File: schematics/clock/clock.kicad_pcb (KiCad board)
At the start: 2 copper layers, 102 x 96 mm, 25 parts, among them J1 Bus, J2 Bus, SW1 RUN, SW2 PULSE, U1 NE556, U2 74LS27, U3 74LS27

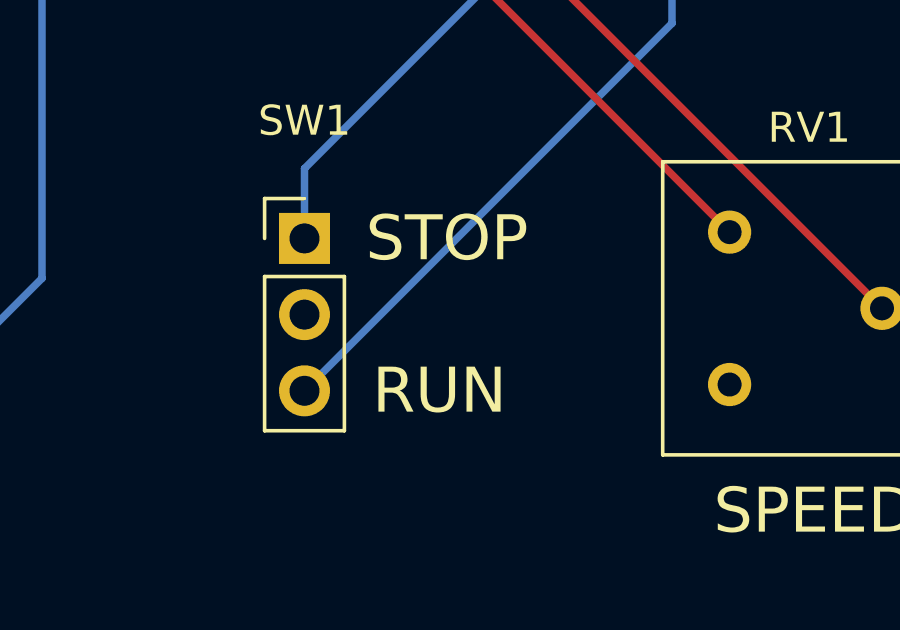
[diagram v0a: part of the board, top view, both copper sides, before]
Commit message: swap labels on Clock Module RUN/SSTOP switch
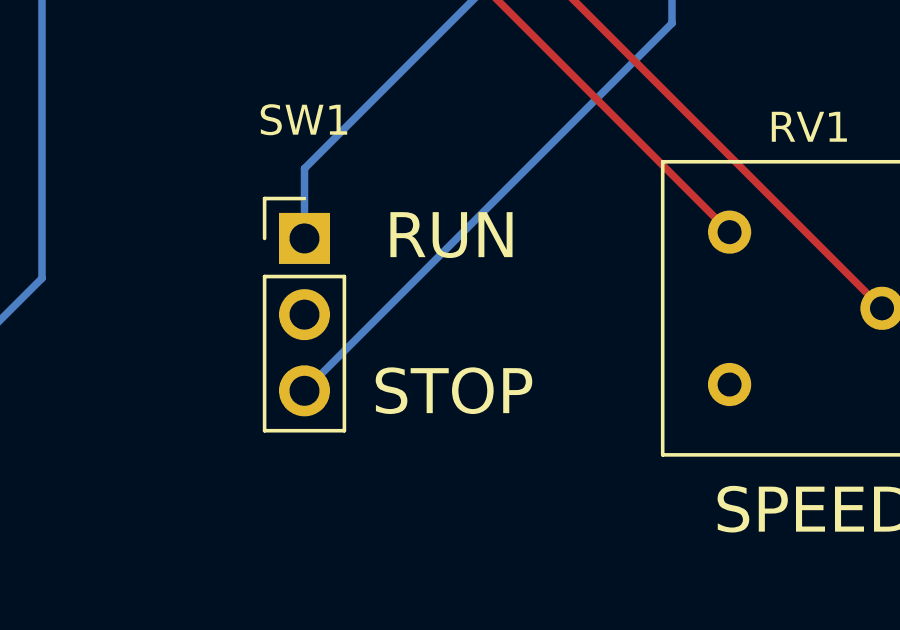
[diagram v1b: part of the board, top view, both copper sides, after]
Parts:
- SW1: value RUN -> STOP
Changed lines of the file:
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@@
 			)
 		)
-		(property "Value" "RUN"
-			(at 4.5 5.08 0)
+		(property "Value" "STOP"
+			(at 4.95 5.13 0)
 			(layer "F.SilkS")
 			(effects
@@
 			)
 		)
-		(property "Field5" "STOP"
-			(at 4.75 0 0)
+		(property "Field5" "RUN"
+			(at 4.9 -0.07 0)
 			(unlocked yes)
 			(layer "F.SilkS")

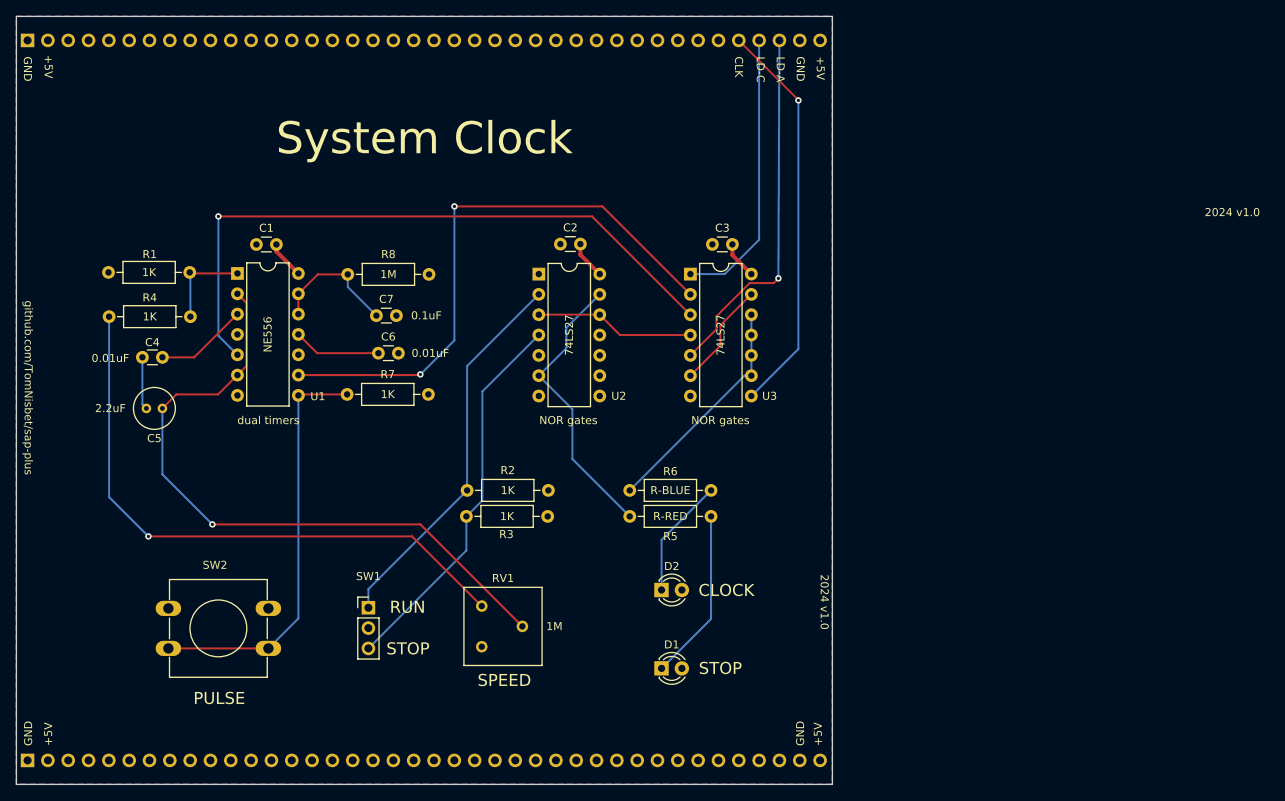
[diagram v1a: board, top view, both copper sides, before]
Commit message: clock module 2.0 - adds clock divider
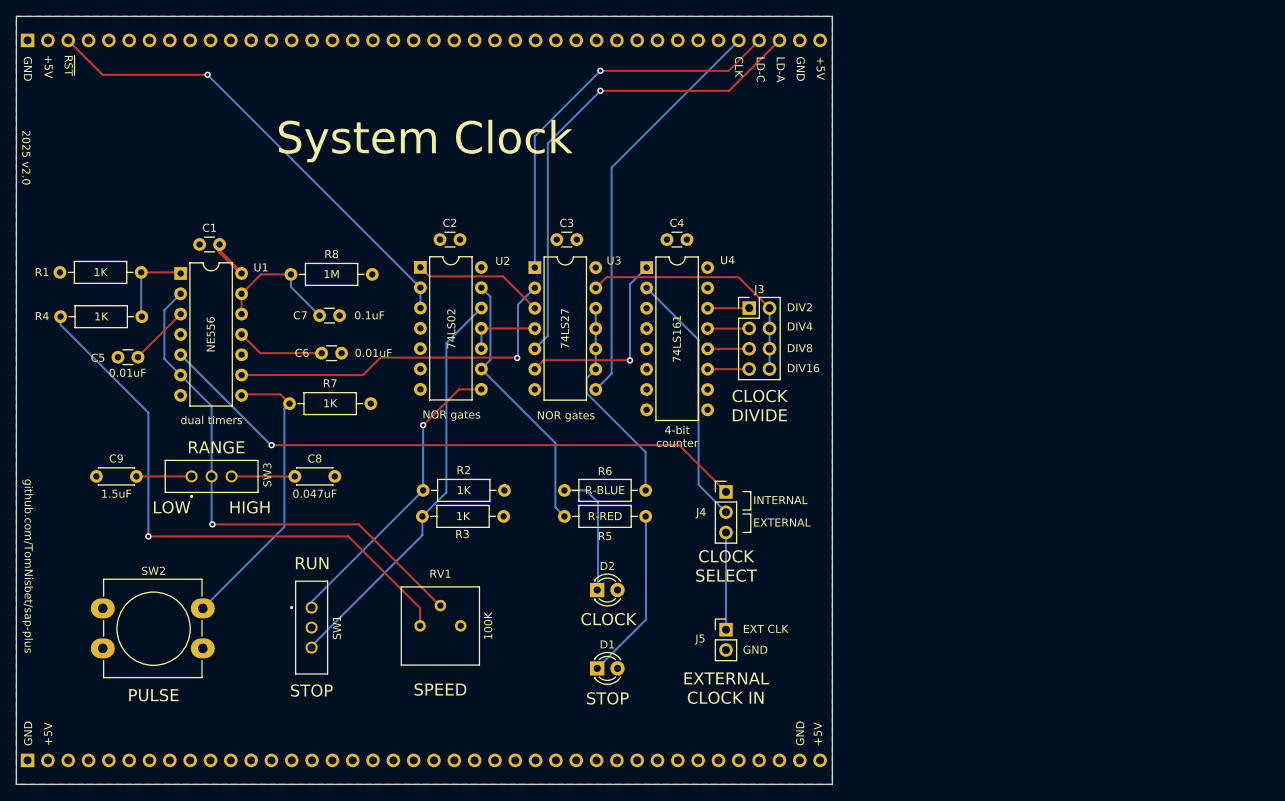
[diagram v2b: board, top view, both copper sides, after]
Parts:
- added C4: 0.1uF, Capacitor_THT:C_Disc_D3.0mm_W1.6mm_P2.50mm, F.Cu at (166.3, 70.9)
- added C9: 1.5uF, Capacitor_THT:C_Disc_D4.3mm_W1.9mm_P5.00mm, F.Cu at (95.0, 100.5)
- added J3: Conn_02x04_Odd_Even, Connector_PinHeader_2.54mm:PinHeader_2x04_P2.54mm_Vertical, F.Cu at (176.6, 79.5)
- added J4: CLOCK SELECT, Connector_PinHeader_2.54mm:PinHeader_1x03_P2.54mm_Vertical, F.Cu at (173.7, 102.4)
- added J5: EXTERNAL CLOCK IN, Connector_PinHeader_2.54mm:PinHeader_1x02_P2.54mm_Vertical, F.Cu at (173.7, 119.7)
- added SW3: SPDT, mySwitches:SW_EG1218, F.Cu at (109.4, 100.5)
- added U4: 74LS161, Package_DIP:DIP-16_W7.62mm, F.Cu at (163.8, 74.4)
- C8: renamed from C5; value 2.2uF -> 0.047uF; footprint Capacitor_THT:C_Radial_D5.0mm_H5.0mm_P2.00mm -> Capacitor_THT:C_Disc_D4.3mm_W1.9mm_P5.00mm
- RV1: value 1M -> 100K; footprint Potentiometer_THT:Potentiometer_Bourns_3386F_Vertical -> Potentiometer_THT:Potentiometer_Bourns_3386P_Vertical
- SW1: footprint Connector_PinHeader_2.54mm:PinHeader_1x03_P2.54mm_Vertical -> mySwitches:SW_EG1218
- SW2: footprint Button_Switch_THT:SW_PUSH-12mm -> Button_Switch_THT:SW_PUSH-12mm_Wuerth-430476085716
- U2: value 74LS27 -> 74LS02
- moved U3 19.5 mm to (149.8, 74.4)
- moved C3 19.5 mm to (152.6, 70.9)
- moved C8 18.6 mm to (119.8, 100.5), turned to 0 degrees
- moved C2 15.1 mm to (137.9, 70.9)
- moved U2 14.8 mm to (135.5, 74.4)
- moved SW2 8.20 mm to (95.8, 117.0)
- moved R5 8.17 mm to (153.5, 105.5)
- moved R6 8.17 mm to (153.5, 102.2)
- moved D1 8.05 mm to (157.6, 124.5)
- moved D2 8.05 mm to (157.6, 114.7)
- moved SW1 7.52 mm to (121.9, 119.4), turned to -90 degrees
- moved R7 7.29 mm to (129.3, 91.4)
- moved R8 7.10 mm to (129.5, 75.2)
- moved C1 7.10 mm to (107.9, 71.5)
- moved C6 7.10 mm to (123.2, 85.1)
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- renumbered C4 to C5
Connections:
- C8 pad 1: Net-(U1A-THR) -> Net-(SW3-C)
- J1 pad 3: unconnected-(J1-Pin_3-Pad3) -> ~{RST}
- R6 pad 1: Net-(R6-Pad1) -> Net-(D2-K)
- R6 pad 2: Net-(D2-K) -> Net-(R6-Pad2)
- RV1 pad 2: Net-(U1A-THR) -> Net-(SW3-B)
- SW2 pad 1: GND -> Net-(U1B-TR)
- SW2 pad 2: Net-(U1B-TR) -> GND
- U1 pad 2: Net-(U1A-THR) -> Net-(SW3-B)
- U1 pad 5: astable -> /INT
- U1 pad 6: Net-(U1A-THR) -> Net-(SW3-B)
- U2 pad 1: GND -> /RST
- U2 pad 10: GND -> ~{run}-stop
- U2 pad 11: GND -> ~{run}-stop
- U2 pad 12: ~{run}-stop -> Net-(SW1-C)
- U2 pad 2: Net-(SW1-A) -> ~{RST}
- U2 pad 3: ~{run}-stop -> ~{RST}
- U2 pad 4: Net-(SW1-C) -> unconnected-(U2-Pad4)
- U2 pad 6: Net-(R5-Pad1) -> GND
- U2 pad 8: unconnected-(U2-Pad8) -> Net-(SW1-A)
- U2 pad 9: GND -> Net-(R5-Pad1)
- U3 pad 10: Net-(R6-Pad1) -> Net-(R6-Pad2)
- U3 pad 11: Net-(R6-Pad1) -> Net-(R6-Pad2)
- U3 pad 12: Net-(R6-Pad1) -> Net-(R6-Pad2)
- U3 pad 13: Net-(U3-Pad13) -> astable
- U3 pad 3: astable -> /RST
- U3 pad 6: Net-(U3-Pad13) -> Net-(U4-~{MR})
- U3 pad 9: Net-(R6-Pad1) -> Net-(R6-Pad2)
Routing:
- net Net-(U1A-THR): track 83.3 -> 0.00 mm, vias 1 -> 0
- net /INT: track 0.00 -> 75.3 mm, vias 0 -> 1
- net Net-(SW3-B): track 0.00 -> 64.9 mm, vias 0 -> 1
- net ~{RST}: track 0.00 -> 59.4 mm, vias 0 -> 1
- net astable: track 82.4 -> 31.5 mm, vias 1 -> 0
- net Net-(J4-Pin_2): track 0.00 -> 32.1 mm
- net Net-(R6-Pad1): track 28.8 -> 0.00 mm
- net single: track 72.1 -> 45.0 mm, vias 2 -> 1
- net Net-(R6-Pad2): track 0.00 -> 26.3 mm
- net Net-(U4-~{MR}): track 0.00 -> 24.8 mm, vias 0 -> 1
- net /RST: track 0.00 -> 16.4 mm
- net Net-(U1B-TR): track 51.8 -> 36.6 mm
- net LD-ACT: track 45.8 -> 60.6 mm
- net LD-CLK: track 35.3 -> 49.4 mm, vias 0 -> 1
- net Net-(U3-Pad13): track 13.3 -> 0.00 mm
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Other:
- board text added: "2025 v${REVISION}"
- board text added: "4-bit counter"
- board text added: "CLOCK DIVIDE"
- board text added: "CLOCK SELECT"
- board text added: "DIV16"
- board text added: "DIV2"
- board text added: "DIV4"
- board text added: "DIV8"
- board text added: "EXT CLK"
- board text added: "EXTERNAL"
- board text added: "EXTERNAL CLOCK IN"
- board text added: "HIGH"
- board text added: "INTERNAL"
- board text added: "LOW"
- board text added: "RANGE"
- board text added: "STOP"
- board text added: "~{RST}"
- board text removed: "2024 v${REVISION}"
- board text removed: "2024 v1.0"
